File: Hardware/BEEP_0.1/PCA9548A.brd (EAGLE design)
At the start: 42.9 x 34.3 mm, 16 parts, among them IC1 PCA9548A

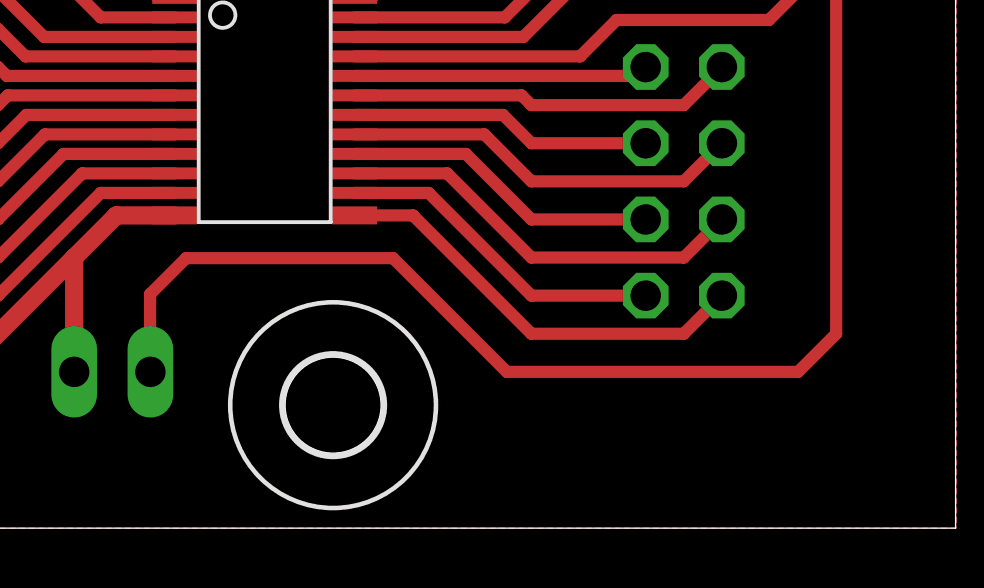
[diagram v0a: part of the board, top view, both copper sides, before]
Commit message: enlarge Clearence to 10mil created some pdf files for the boards
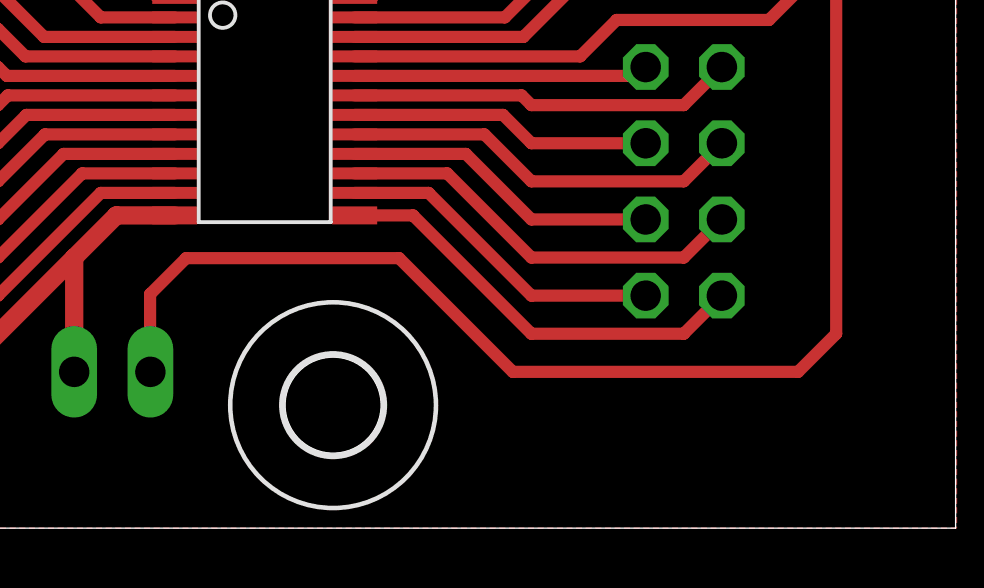
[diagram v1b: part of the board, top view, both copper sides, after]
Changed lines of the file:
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@@
 </class>
 </classes>
-<designrules name="default">
+<designrules name="default *">
 <description language="de">&lt;b&gt;EAGLE Design Rules&lt;/b&gt;
 &lt;p&gt;
@@
 <param name="mtCopper" value="0.035mm 0.035mm 0.035mm 0.035mm 0.035mm 0.035mm 0.035mm 0.035mm 0.035mm 0.035mm 0.035mm 0.035mm 0.035mm 0.035mm 0.035mm 0.035mm"/>
 <param name="mtIsolate" value="1.5mm 0.15mm 0.2mm 0.15mm 0.2mm 0.15mm 0.2mm 0.15mm 0.2mm 0.15mm 0.2mm 0.15mm 0.2mm 0.15mm 0.2mm"/>
-<param name="mdWireWire" value="8mil"/>
-<param name="mdWirePad" value="8mil"/>
+<param name="mdWireWire" value="10mil"/>
+<param name="mdWirePad" value="10mil"/>
 <param name="mdWireVia" value="8mil"/>
 <param name="mdPadPad" value="8mil"/>
@@
 <wire x1="31.89" y1="26.92" x2="31.99" y2="26.8" width="0.4064" layer="1"/>
 <wire x1="23.63" y1="26.17" x2="23" y2="26.8" width="0.4064" layer="1"/>
-<wire x1="37.6" y1="5.21" x2="27.89" y2="5.21" width="0.4064" layer="1"/>
-<wire x1="27.89" y1="5.21" x2="24.1" y2="9" width="0.4064" layer="1"/>
-<wire x1="24.1" y1="9" x2="17.2" y2="9" width="0.4064" layer="1"/>
+<wire x1="37.6" y1="5.21" x2="28.09" y2="5.21" width="0.4064" layer="1"/>
+<wire x1="28.09" y1="5.21" x2="24.3" y2="9" width="0.4064" layer="1"/>
+<wire x1="24.3" y1="9" x2="17.2" y2="9" width="0.4064" layer="1"/>
 <wire x1="23" y1="26.8" x2="26.17" y2="26.8" width="0.4064" layer="1"/>
 <wire x1="26.17" y1="26.8" x2="31.99" y2="26.8" width="0.4064" layer="1"/>
@@
 <contactref element="RESET" pad="2"/>
 <contactref element="R4" pad="1"/>
-<wire x1="16.82" y1="16.375" x2="12.465" y2="16.375" width="0.4064" layer="1"/>
 <wire x1="12.465" y1="16.375" x2="10.93" y2="17.91" width="0.4064" layer="1"/>
 <wire x1="7.12" y1="21.4" x2="7.44" y2="21.72" width="0.4064" layer="1"/>
@@
 <wire x1="7.12" y1="19.18" x2="7.12" y2="21.4" width="0.4064" layer="1"/>
 <wire x1="4.58" y1="21.72" x2="7.44" y2="21.72" width="0.4064" layer="1"/>
+<wire x1="16.82" y1="16.375" x2="12.465" y2="16.375" width="0.4064" layer="1"/>
 </signal>
 <signal name="SD0">
 <contactref element="IC1" pad="SD0"/>
-<wire x1="16.82" y1="15.725" x2="11.845" y2="15.725" width="0.4064" layer="1"/>
 <wire x1="11.845" y1="15.725" x2="10.93" y2="16.64" width="0.4064" layer="1"/>
 <wire x1="10.93" y1="16.64" x2="5.85" y2="16.64" width="0.4064" layer="1"/>
 <contactref element="JP3" pad="2"/>
 <wire x1="5.85" y1="16.64" x2="4.58" y2="15.37" width="0.4064" layer="1"/>
+<wire x1="16.82" y1="15.725" x2="11.845" y2="15.725" width="0.4064" layer="1"/>
 </signal>
 <signal name="SC0">
 <contactref element="IC1" pad="SC0"/>
-<wire x1="16.82" y1="15.075" x2="11.225" y2="15.075" width="0.4064" layer="1"/>
 <wire x1="11.225" y1="15.075" x2="10.93" y2="15.37" width="0.4064" layer="1"/>
 <contactref element="JP3" pad="1"/>
 <wire x1="10.93" y1="15.37" x2="7.12" y2="15.37" width="0.4064" layer="1"/>
+<wire x1="16.82" y1="15.075" x2="11.225" y2="15.075" width="0.4064" layer="1"/>
 </signal>
 <signal name="SD1">
 <contactref element="IC1" pad="SD1"/>
-<wire x1="16.82" y1="14.425" x2="11.255" y2="14.425" width="0.4064" layer="1"/>
 <wire x1="11.255" y1="14.425" x2="10.93" y2="14.1" width="0.4064" layer="1"/>
 <wire x1="10.93" y1="14.1" x2="5.85" y2="14.1" width="0.4064" layer="1"/>
 <contactref element="JP3" pad="4"/>
 <wire x1="5.85" y1="14.1" x2="4.58" y2="12.83" width="0.4064" layer="1"/>
+<wire x1="16.82" y1="14.425" x2="11.255" y2="14.425" width="0.4064" layer="1"/>
 </signal>
 <signal name="SC1">
 <contactref element="IC1" pad="SC1"/>
-<wire x1="16.82" y1="13.775" x2="11.875" y2="13.775" width="0.4064" layer="1"/>
 <wire x1="11.875" y1="13.775" x2="10.93" y2="12.83" width="0.4064" layer="1"/>
 <contactref element="JP3" pad="3"/>
 <wire x1="10.93" y1="12.83" x2="7.12" y2="12.83" width="0.4064" layer="1"/>
+<wire x1="16.82" y1="13.775" x2="11.875" y2="13.775" width="0.4064" layer="1"/>
 </signal>
 <signal name="SD2">
 <contactref element="IC1" pad="SD2"/>
-<wire x1="16.82" y1="13.125" x2="12.495" y2="13.125" width="0.4064" layer="1"/>
 <wire x1="12.495" y1="13.125" x2="10.93" y2="11.56" width="0.4064" layer="1"/>
 <wire x1="10.93" y1="11.56" x2="5.85" y2="11.56" width="0.4064" layer="1"/>
 <contactref element="JP3" pad="6"/>
 <wire x1="5.85" y1="11.56" x2="4.58" y2="10.29" width="0.4064" layer="1"/>
+<wire x1="16.82" y1="13.125" x2="12.495" y2="13.125" width="0.4064" layer="1"/>
 </signal>
 <signal name="SC2">
 <contactref element="IC1" pad="SC2"/>
-<wire x1="16.82" y1="12.475" x2="13.115" y2="12.475" width="0.4064" layer="1"/>
 <wire x1="13.115" y1="12.475" x2="10.93" y2="10.29" width="0.4064" layer="1"/>
 <contactref element="JP3" pad="5"/>
 <wire x1="10.93" y1="10.29" x2="7.12" y2="10.29" width="0.4064" layer="1"/>
+<wire x1="16.82" y1="12.475" x2="13.115" y2="12.475" width="0.4064" layer="1"/>
 </signal>
 <signal name="SD3">
 <contactref element="IC1" pad="SD3"/>
-<wire x1="16.82" y1="11.825" x2="13.735" y2="11.825" width="0.4064" layer="1"/>
 <wire x1="13.735" y1="11.825" x2="10.93" y2="9.02" width="0.4064" layer="1"/>
 <wire x1="10.93" y1="9.02" x2="5.85" y2="9.02" width="0.4064" layer="1"/>
 <contactref element="JP3" pad="8"/>
 <wire x1="5.85" y1="9.02" x2="4.58" y2="7.75" width="0.4064" layer="1"/>
+<wire x1="16.82" y1="11.825" x2="13.735" y2="11.825" width="0.4064" layer="1"/>
 </signal>
 <signal name="SC3">
 <contactref element="IC1" pad="SC3"/>
-<wire x1="16.82" y1="11.175" x2="14.355" y2="11.175" width="0.4064" layer="1"/>
 <wire x1="14.355" y1="11.175" x2="10.93" y2="7.75" width="0.4064" layer="1"/>
 <contactref element="JP3" pad="7"/>
 <wire x1="10.93" y1="7.75" x2="7.12" y2="7.75" width="0.4064" layer="1"/>
+<wire x1="16.82" y1="11.175" x2="14.355" y2="11.175" width="0.4064" layer="1"/>
 </signal>
 <signal name="SC7">
@@
 <wire x1="14.355" y1="17.025" x2="12.2" y2="19.18" width="0.4064" layer="1"/>
 <contactref element="IC1" pad="A1"/>
-<wire x1="16.82" y1="17.025" x2="14.355" y2="17.025" width="0.4064" layer="1"/>
 <wire x1="12.2" y1="24.26" x2="12.2" y2="19.18" width="0.4064" layer="1"/>
 <contactref element="A01" pad="3"/>
 <wire x1="12.2" y1="24.26" x2="16.01" y2="24.26" width="0.4064" layer="1"/>
+<wire x1="16.82" y1="17.025" x2="14.355" y2="17.025" width="0.4064" layer="1"/>
 </signal>
 </signals>
+<errors>
+</errors>
 </board>
 </drawing>

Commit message: Add branding ;) enhance PCBs finish Easy RGB Board add Texas Instruments libray from Element 14 add dxf import ulp for eagle add Script for easy eagle export to pdf for etching minor cleanup
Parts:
- added U$1: LOGO-COPPER4, Branding:COPPER4
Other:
- board text added: "PCA9548A v0.1.1"
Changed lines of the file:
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@@
 <layer number="43" name="vRestrict" color="2" fill="10" visible="yes" active="yes"/>
 <layer number="44" name="Drills" color="7" fill="1" visible="no" active="yes"/>
-<layer number="45" name="Holes" color="7" fill="1" visible="no" active="yes"/>
+<layer number="45" name="Holes" color="7" fill="1" visible="yes" active="yes"/>
 <layer number="46" name="Milling" color="3" fill="1" visible="no" active="yes"/>
 <layer number="47" name="Measures" color="7" fill="1" visible="no" active="yes"/>
-<layer number="48" name="Document" color="7" fill="1" visible="yes" active="yes"/>
-<layer number="49" name="Reference" color="7" fill="1" visible="yes" active="yes"/>
+<layer number="48" name="Document" color="7" fill="1" visible="no" active="yes"/>
+<layer number="49" name="Reference" color="7" fill="1" visible="no" active="yes"/>
 <layer number="51" name="tDocu" color="7" fill="1" visible="yes" active="yes"/>
 <layer number="52" name="bDocu" color="7" fill="1" visible="yes" active="yes"/>
@@
 <layer number="97" name="Info" color="7" fill="1" visible="no" active="no"/>
 <layer number="98" name="Guide" color="6" fill="1" visible="no" active="no"/>
+<layer number="100" name="tCName" color="7" fill="1" visible="yes" active="yes"/>
+<layer number="101" name="bCName" color="7" fill="1" visible="yes" active="yes"/>
 </layers>
 <board>
@@
 <text x="36.5" y="22.7" size="1.778" layer="26" rot="MR180">SDA</text>
 <text x="36.5" y="20.1" size="1.778" layer="26" rot="MR180">SCL</text>
+<text x="35" y="0.8" size="0.8128" layer="100">PCA9548A
+v0.1.1</text>
+<polygon width="0.4064" layer="41">
+<vertex x="41" y="3.4"/>
+<vertex x="41" y="-0.1"/>
+<vertex x="26.1" y="-0.1"/>
+<vertex x="26.1" y="3.4"/>
+</polygon>
 </plain>
 <attributes>
@@
 <element name="U$3" library="holes" package="3,2" value="" x="4.1" y="30.2"/>
 <element name="U$4" library="holes" package="3,2" value="" x="38.7" y="30.1"/>
+<element name="U$1" library="Branding" package="COPPER4" value="LOGO-COPPER4" x="27.3" y="0.9"/>
 </elements>
 <signals>
@@
 </signal>
 </signals>
-<errors>
-</errors>
 </board>
 </drawing>
+<compatibility>
+<note version="6.3" minversion="6.2.2" severity="warning">
+Since Version 6.2.2 text objects can contain more than one line,
+which will not be processed correctly with this version.
+</note>
+</compatibility>
 </eagle>
